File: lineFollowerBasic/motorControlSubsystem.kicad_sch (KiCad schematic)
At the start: 0 parts

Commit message: Tu mensaje de commit
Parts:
- added C10, C9: 100 uF, Capacitor_THT:CP_Axial_L10.0mm_D4.5mm_P15.00mm_Horizontal, symbol Device:C_Polarized
- added C3, C4: 0.1 uF, Capacitor_THT:CP_Axial_L10.0mm_D4.5mm_P15.00mm_Horizontal, symbol Device:C_Polarized
- added C5, C6, C7, C8: 1 uF, Capacitor_THT:CP_Axial_L10.0mm_D4.5mm_P15.00mm_Horizontal, symbol Device:C_Polarized
- added D1, D2: D, symbol Device:D
- added M1: Motor_DC, symbol Motor:Motor_DC
- added Q1, Q2, Q3, Q4: IRLZ44N, Package_TO_SOT_THT:TO-220-3_Vertical, symbol Transistor_FET:IRLZ44N
- added R1, R2: 4.7k, Resistor_THT:R_Axial_DIN0204_L3.6mm_D1.6mm_P5.08mm_Horizontal, symbol Device:R
- added R3, R4, R5, R6: 220, Resistor_THT:R_Axial_DIN0204_L3.6mm_D1.6mm_P5.08mm_Horizontal, symbol Device:R
- added U5: ATmega328-P, Package_DIP:DIP-28_W7.62mm, symbol MCU_Microchip_ATmega:ATmega328-P
- added U6, U7: IR2110, Package_DIP:DIP-14_W7.62mm, symbol Driver_FET:IR2110
- added U8: INA219BxD, Package_SO:SOIC-8_3.9x4.9mm_P1.27mm, symbol Sensor_Energy:INA219BxD
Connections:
- new net: Q2.1 (G), R4.1
- new net: R4.2, U6.1 (LO)
- new net: Q3.1 (G), R5.1
- new net: C8.2, M1.1 (+), Q3.3 (S), Q4.2 (D), U7.5 (VS), U8.8 (IN+)
- new net: Q4.1 (G), R6.1
- new net: R6.2, U7.1 (LO)
- new net: U5.15 (PB1), U7.10 (HIN)
- new net: U5.16 (PB2), U7.12 (LIN)
- new net: C8.1, D2.1 (K), U7.6 (VB)
- new net: R5.2, U7.7 (HO)
- new net: C4.1, U5.7 (VCC), U7.9 (VDD), U8.5 (VS)
- new net: U5.11 (PD5), U6.10 (HIN)
- new net: U5.12 (PD6), U6.12 (LIN)
- new net: R1.2, U5.27 (PC4), U8.4 (SCL)
- new net: R2.2, U5.28 (PC5), U8.3 (SDA)
- new net: C7.2, M1.2 (-), Q1.3 (S), Q2.2 (D), U6.5 (VS), U8.7 (IN-)
- new net: C7.1, D1.1 (K), U6.6 (VB)
- new net: Q1.1 (G), R3.1
- new net: R3.2, U6.7 (HO)
- new net: C3.1, U6.9 (VDD)
- new net +15: C10.1, C5.1, C6.1, C9.1, D1.2 (A), D2.2 (A), Q1.2 (D), Q3.2 (D), R1.1, R2.1, U6.3 (VCC), U7.3 (VCC)
- new net GNDREF: C10.2, C3.2, C4.2, C5.2, C6.2, C9.2, Q2.3 (S), Q4.3 (S), U5.22 (GND), U5.8 (GND), U6.11 (SD), U6.13 (VSS), U6.2 (COM), U7.11 (SD), U7.13 (VSS), U7.2 (COM), U8.1 (A1), U8.2 (A0), U8.6 (GND)

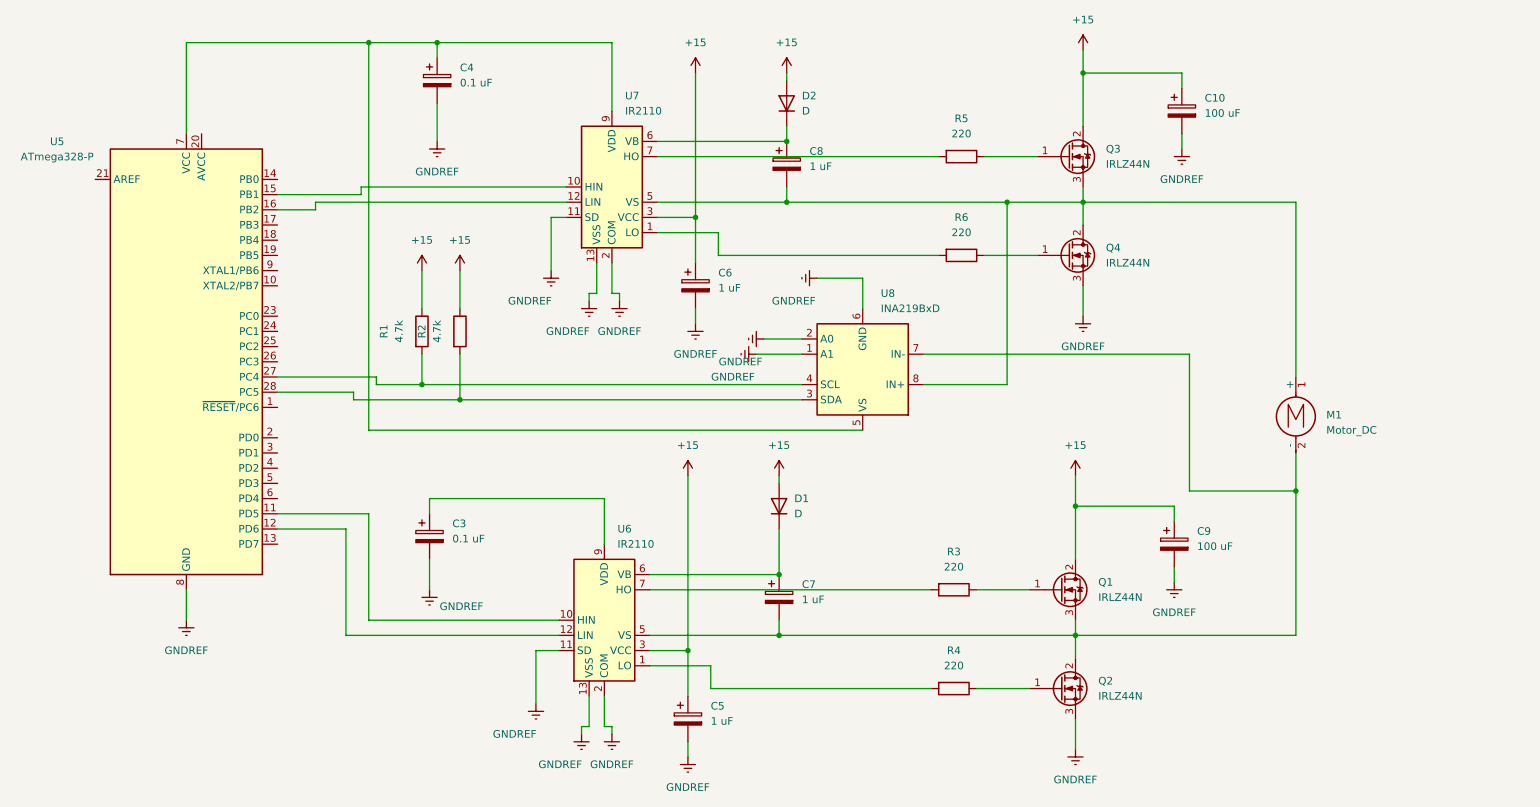
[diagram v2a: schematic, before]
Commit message: Deleted extra ATMEGAs, added labels
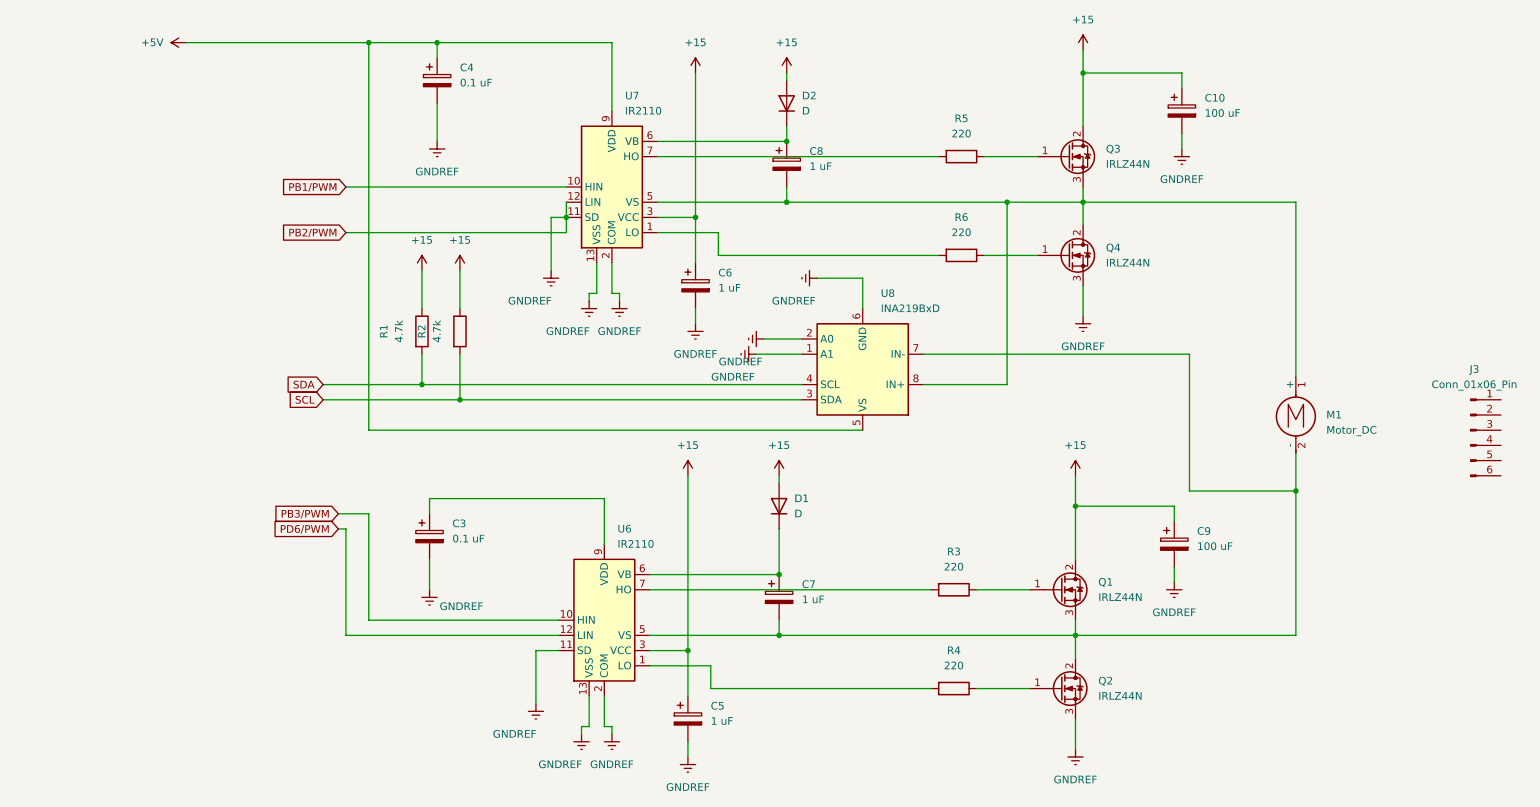
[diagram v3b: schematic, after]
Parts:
- removed U5: ATmega328-P, Package_DIP:DIP-28_W7.62mm, symbol MCU_Microchip_ATmega:ATmega328-P
- added J3: Conn_01x06_Pin, symbol Connector:Conn_01x06_Pin
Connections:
- net GNDREF: now also U7.12 (LIN)
- net PB1/PWM: now reaches U7.10 (HIN)
- net +5V: now reaches C4.1, U7.9 (VDD), U8.5 (VS)
- net PB3/PWM: now reaches U6.10 (HIN)
- net PD6/PWM: now reaches U6.12 (LIN)
- net SDA: now reaches R1.2, U8.4 (SCL)
- net SCL: now reaches R2.2, U8.3 (SDA)

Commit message: Definicion de capacitores y diodos de proteccion
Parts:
- removed M1: Motor_DC, symbol Motor:Motor_DC
- C7, C8: value 1 uF -> 0.1 uF
- J3: footprint (none) -> Connector_Molex:Molex_Mini-Fit_Jr_5566-06A2_2x03_P4.20mm_Vertical
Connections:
- net at C8.2, Q3.3 (S), Q4.2 (D)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: now also J3.1 (Pin_1)
- net at C7.2, Q1.3 (S), Q2.2 (D)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: now also J3.6 (Pin_6)
- net +15 renamed +5
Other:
- moved on the sheet: J3
